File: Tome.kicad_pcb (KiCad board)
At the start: 2 copper layers, 25 x 25 mm, 134 parts, among them J1 USB_C_Receptacle_USB2.0_14P, J2 [battery], J3 SD_Card_Receptacle, J4 [bootstrap jumper], J5 AudioJack3, J6 FPC Connector, J7 FPC Connector, J8 FFC Connector, J9 FFC Connector, Q1 DMG3415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

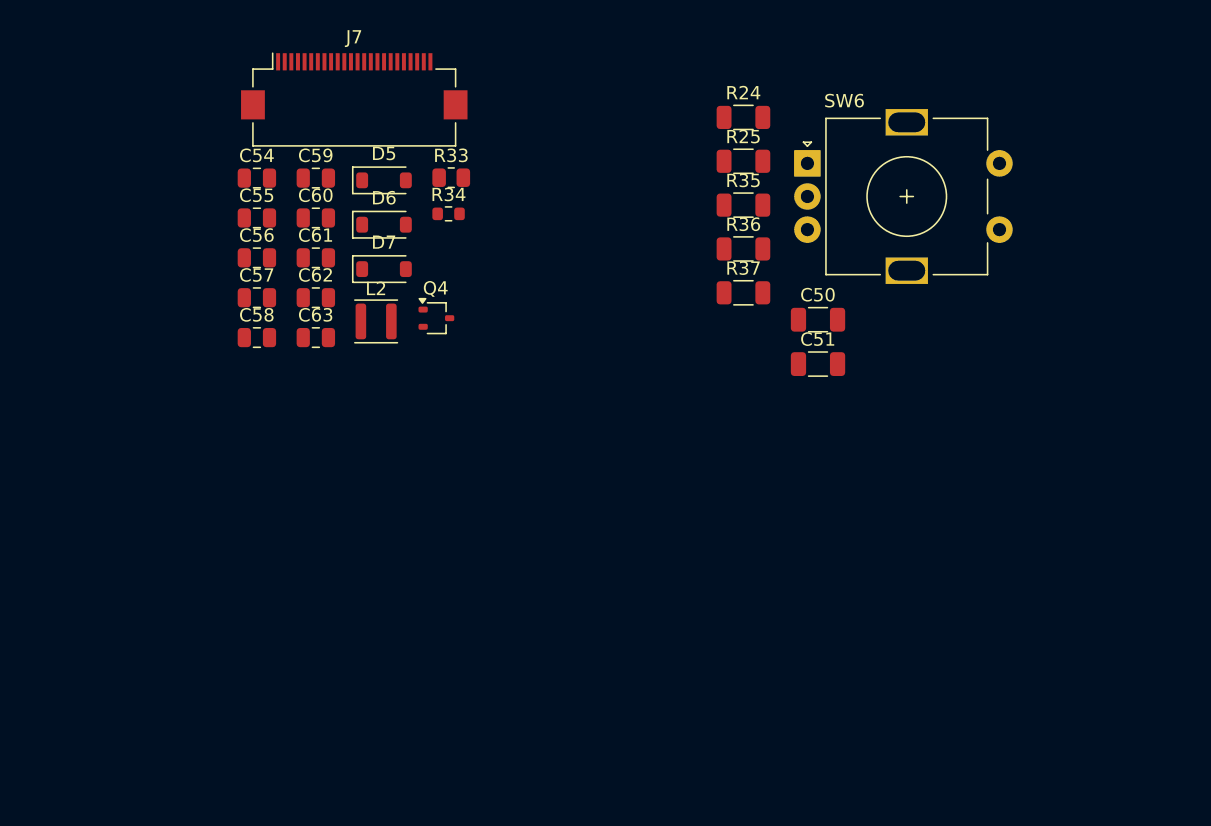
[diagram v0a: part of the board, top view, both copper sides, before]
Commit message: different encoder board layout
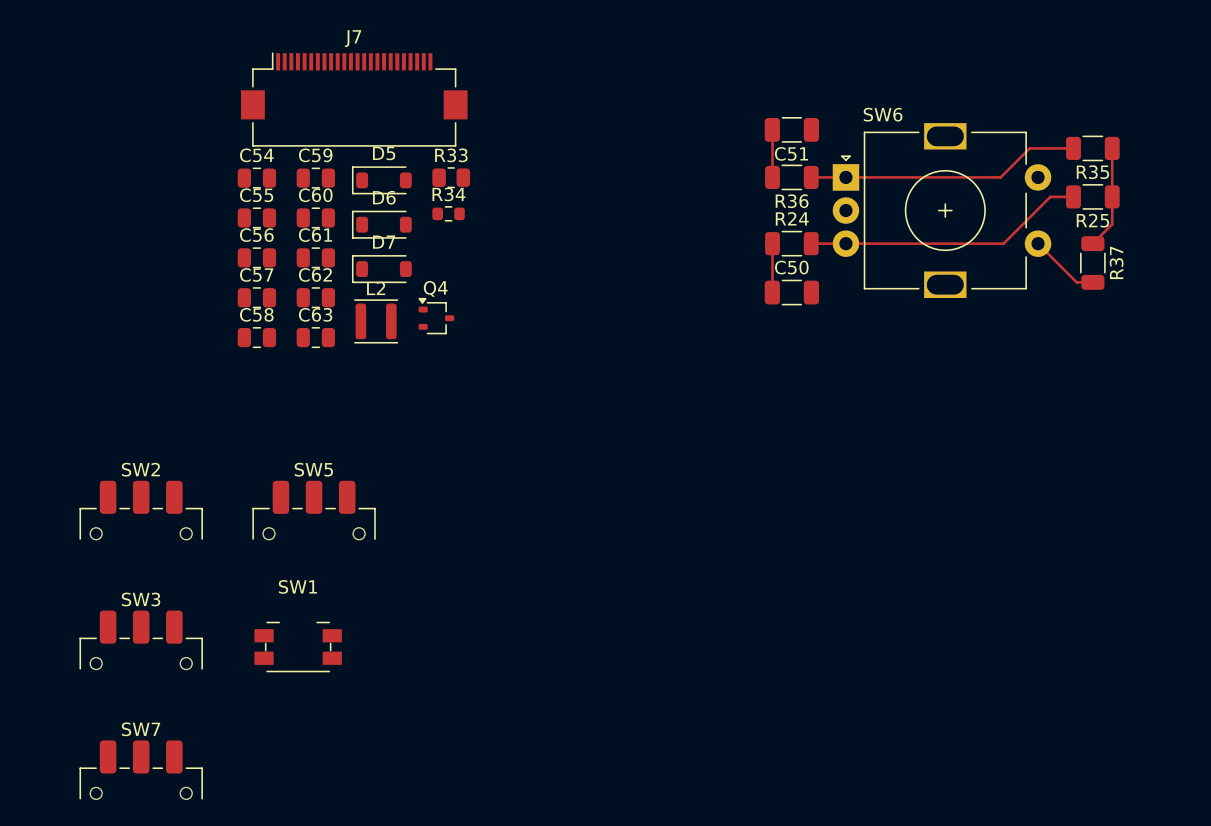
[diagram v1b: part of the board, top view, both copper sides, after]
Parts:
- added SW1: [reset button], Button_Switch_SMD:Panasonic_EVQPUK_EVQPUB, F.Cu at (82.3, 135.2)
- added SW2: SW_SPST, Button_Switch_SMD:SW_SPDT_CK_JS102011SAQN, F.Cu at (70.4, 126.6)
- added SW3: SW_SPST, Button_Switch_SMD:SW_SPDT_CK_JS102011SAQN, F.Cu at (70.4, 136.4)
- added SW5: SW_SPST, Button_Switch_SMD:SW_SPDT_CK_JS102011SAQN, F.Cu at (83.5, 126.6)
- added SW7: SW_SPST, Button_Switch_SMD:SW_SPDT_CK_JS102011SAQN, F.Cu at (70.4, 146.2)
- moved R35 26.7 mm to (142.3, 97.5), turned to 180 degrees
- moved R25 26.5 mm to (142.3, 101.2), turned to 180 degrees
- moved R37 26.5 mm to (142.3, 106.2), turned to -90 degrees
- moved C51 17.8 mm to (119.6, 96.1)
- moved R24 10.2 mm to (119.6, 104.7)
- moved R36 6.52 mm to (119.6, 99.7)
- moved SW6 3.10 mm to (123.7, 99.7)
- moved C50 2.84 mm to (119.6, 108.4)
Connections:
- R32 pad 1: Net-(R28-Pad2) -> ENCODER_2_A
- R32 pad 2: ENCODER_2_A -> Net-(R28-Pad2)
- R36 pad 1: Net-(R35-Pad2) -> ENCODER_1_A
- R36 pad 2: ENCODER_1_A -> Net-(R35-Pad2)
- SW4 pad MP: GND -> (no net)
- SW6 pad MP: (no net) -> GND
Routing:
- net Net-(R24-Pad2): track 0.00 -> 21.3 mm
- net Net-(R35-Pad2): track 0.00 -> 20.7 mm
- net +3.3VP: track 8.57 -> 16.4 mm
- net ENCODER_1_PUSH: track 0.00 -> 5.35 mm
- net ENCODER_1_B: track 0.00 -> 3.70 mm
- net ENCODER_1_A: track 0.00 -> 3.60 mm

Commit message: workshopping encoder board
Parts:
- added J10: Conn_01x02_Pin, Connector_PinHeader_2.00mm:PinHeader_1x02_P2.00mm_Vertical, F.Cu at (132.1, 66.8)
- added J11: Conn_01x02_Pin, Connector_PinHeader_2.00mm:PinHeader_1x02_P2.00mm_Vertical, F.Cu at (76.5, 51.8)
- added J12: Conn_01x02_Pin, Connector_PinHeader_2.00mm:PinHeader_1x02_P2.00mm_Vertical, F.Cu at (136.2, 66.8)
- added J13: Conn_01x02_Pin, Connector_PinHeader_2.00mm:PinHeader_1x02_P2.00mm_Vertical, F.Cu at (80.6, 51.8)
- added J14: Conn_01x02_Pin, Connector_PinHeader_2.00mm:PinHeader_1x02_P2.00mm_Vertical, F.Cu at (140.2, 66.8)
- added J15: Conn_01x02_Pin, Connector_PinHeader_2.00mm:PinHeader_1x02_P2.00mm_Vertical, F.Cu at (84.6, 51.8)
- added J16: Conn_01x02_Pin, Connector_PinHeader_2.00mm:PinHeader_1x02_P2.00mm_Vertical, F.Cu at (144.3, 66.8)
- added J17: Conn_01x02_Pin, Connector_PinHeader_2.00mm:PinHeader_1x02_P2.00mm_Vertical, F.Cu at (88.7, 51.8)
- moved J5 59.6 mm to (91.5, 112.1), turned to 90 degrees
- moved SW1 46.7 mm to (36.0, 129.4)
- moved SW5 46.7 mm to (37.2, 120.8)
- moved SW2 46.7 mm to (24.1, 120.8)
- moved SW3 46.7 mm to (24.1, 130.6)
- moved SW7 46.7 mm to (24.1, 140.4)
- moved C54 23.5 mm to (61.7, 84.0)
- moved C56 23.5 mm to (61.7, 90.0)
- moved C57 23.5 mm to (61.7, 93.0)
- moved D5 23.5 mm to (71.3, 84.2)
- moved D6 23.5 mm to (71.3, 87.5)
- moved J7 23.5 mm to (69.0, 77.1)
- moved L2 23.5 mm to (70.7, 94.8)
- moved C55 23.5 mm to (61.7, 87.0)
- moved C58 23.5 mm to (61.7, 96.0)
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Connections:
- SW6 pad MP: GND -> (no net)
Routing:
- net Net-(R28-Pad2): track 24.7 -> 16.9 mm
- net GND: track 2.69 -> 6.16 mm, vias 2 -> 4
- net ENCODER_2_A: track 2.76 -> 0.00 mm
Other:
- board size 25 x 25 mm -> 153.1 x 139.6 mm
